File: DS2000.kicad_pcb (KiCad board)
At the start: 4 copper layers, 72 x 46 mm, 58 parts, among them J1 USB-C, J3 USB wire, SW1 MUTE, SW2 DEAFEN, SW3 DISCONNECT, U1 USBLC6-2SC6, U2 AP2112K-3.3, U3 RP2350A, U4 W25Q32JVSS, U5 74AHCT1G125, Y1 12MHz

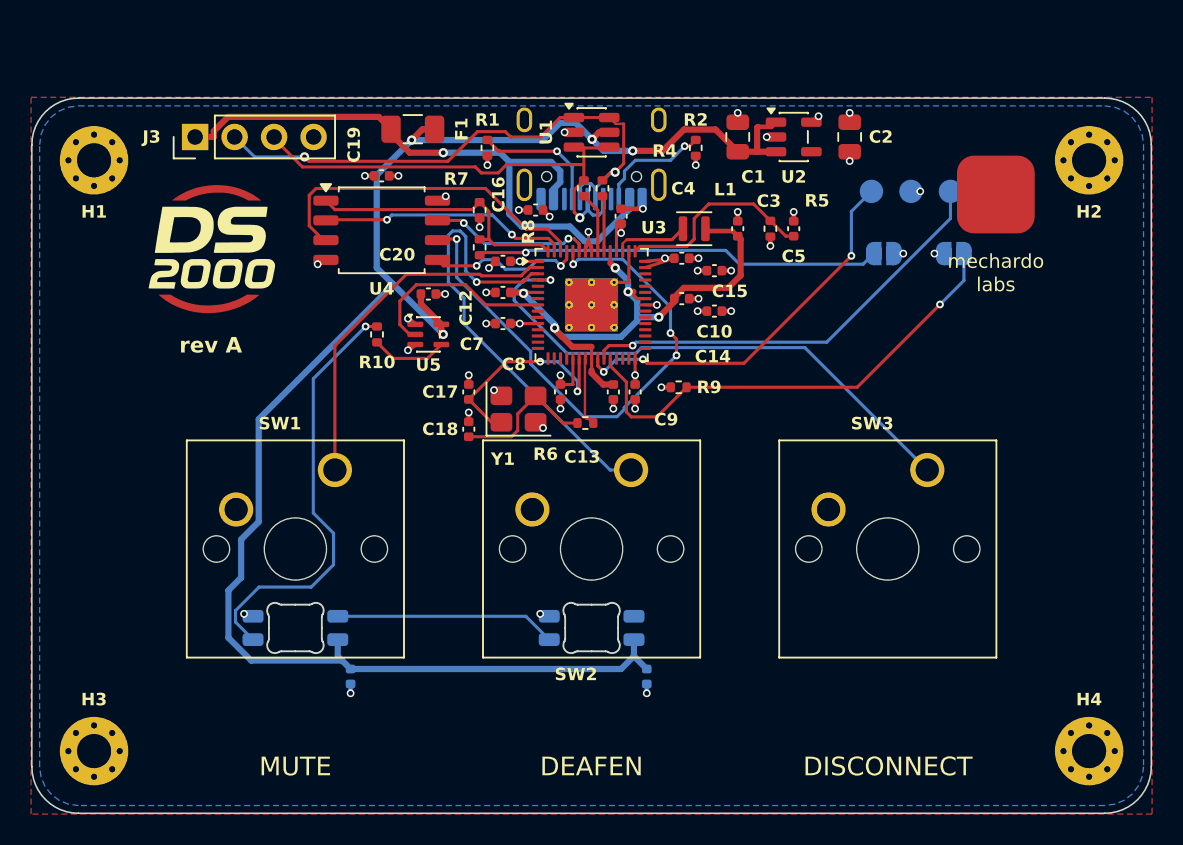
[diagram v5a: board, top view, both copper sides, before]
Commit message: fix: shorten the crystal and flash clock routing, stitch the ground pours
A full review (every net against Raspberry Pi's RP2350 minimal design, every footprint's pinout
against its datasheet) found no wrong connection. It did find routing the autorouter had done
poorly:

- XIN ran 14 mm with two vias. preroute.py now hand-routes the crystal loop as locked tracks with
  the crystal turned under XIN/XOUT so the nets never cross: XIN 7.4 mm, XOUT 2.1 mm, the crystal
  output 4.9 mm, all on F.Cu with no vias. IOVDD pin 20, beside XIN, runs to C8 above it.
- The QSPI clock ran 35.5 mm with four vias. R7, R8 and C16 move out of the corridor between the
  flash and the RP2350; SCLK is now 11 mm with two.

stitch.py ties the F.Cu and B.Cu GND pours to the In1 plane with a 3.5 mm grid of vias wherever
they clear everything else (119 vias). The pipeline keeps an incremental Freerouting pass only
when KiCad's DRC counts fewer unconnected items, and fanout leaves hand-routed pads alone.

DRC: no unconnected pads, no clearance or courtyard errors, full schematic parity.
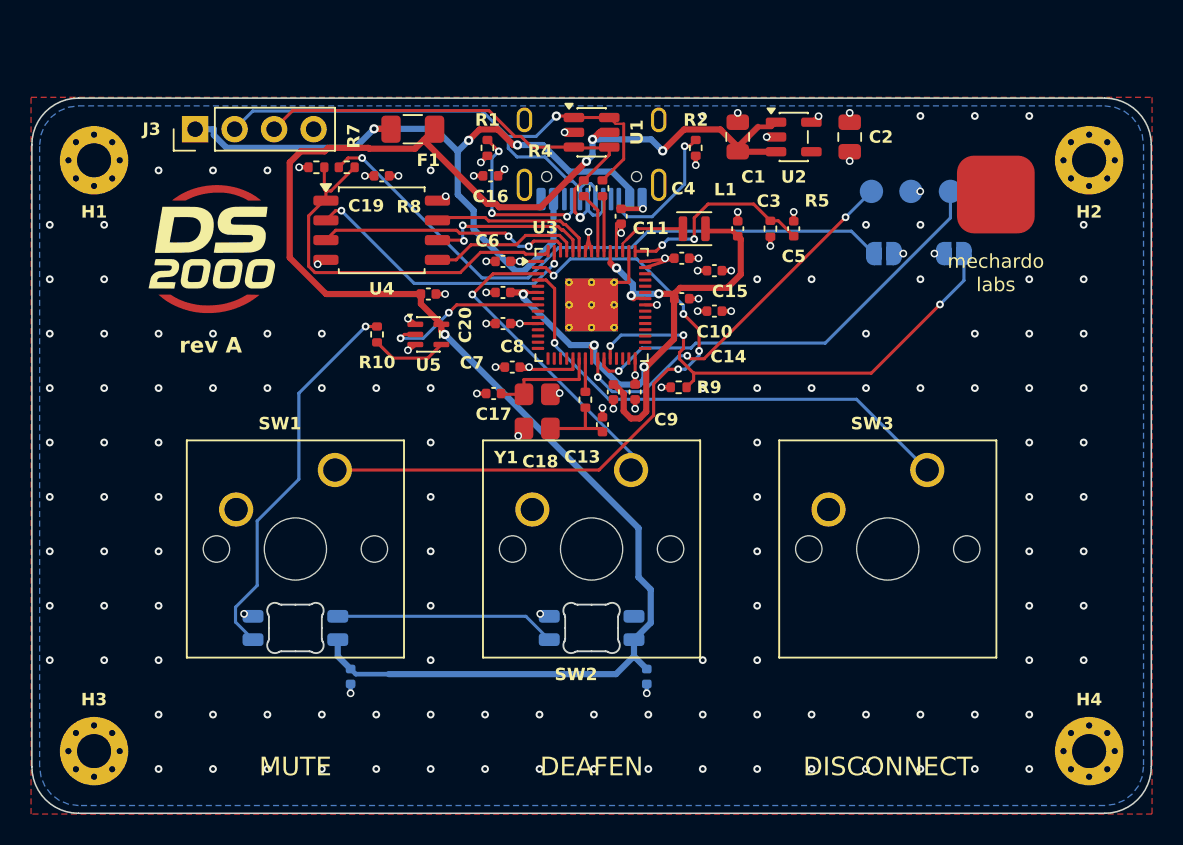
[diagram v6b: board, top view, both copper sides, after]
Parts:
- moved R7 10.9 mm to (82.3, 75.5), turned to 0 degrees
- moved R8 9.98 mm to (84.2, 75.5), turned to 0 degrees
- moved C18 8.61 mm to (100.7, 92.0)
- moved C16 3.64 mm to (93.5, 76.0)
- moved C8 3.49 mm to (94.9, 88.3), turned to 180 degrees
- moved C17 1.60 mm to (93.7, 90.0), turned to 180 degrees
- moved R6 1.50 mm to (99.6, 90.4), turned to 90 degrees
- moved Y1 1.21 mm to (96.5, 91.2), turned to -90 degrees
- moved J3 0.50 mm to (74.5, 73.0)
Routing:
- net Net-(U3-QSPI_SCLK): track 35.5 -> 11.0 mm, vias 4 -> 2
- net Net-(U3-GPIO0): track 23.2 -> 42.5 mm, vias 0 -> 4
- net Net-(JP1-B): track 26.1 -> 39.7 mm
- net Net-(U3-GPIO1): track 29.5 -> 20.3 mm
- net Net-(U3-~{QSPI_SS}): track 17.7 -> 25.7 mm
- net VBUS: track 41.2 -> 48.9 mm, vias 1 -> 3
- net +1V1: track 36.6 -> 43.8 mm, vias 5 -> 6
- net Net-(U3-XIN): track 14.0 -> 7.37 mm, vias 2 -> 0
- net Net-(U3-QSPI_SD2): track 21.8 -> 16.4 mm, vias 0 -> 2
- net Net-(C18-Pad1): track 9.44 -> 4.92 mm
- net /USB_CONN_DM: track 36.0 -> 40.2 mm, vias 2 -> 1
- net Net-(U3-GPIO2): track 35.5 -> 32.2 mm
- net Net-(J1-CC1): track 8.26 -> 11.4 mm, vias 1 -> 3
- net Net-(D1-DIN): track 27.9 -> 24.8 mm
- net +5V: track 108.2 -> 110.8 mm
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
